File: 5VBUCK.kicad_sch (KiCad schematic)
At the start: 1 part, among them U1 LM76005RNPR

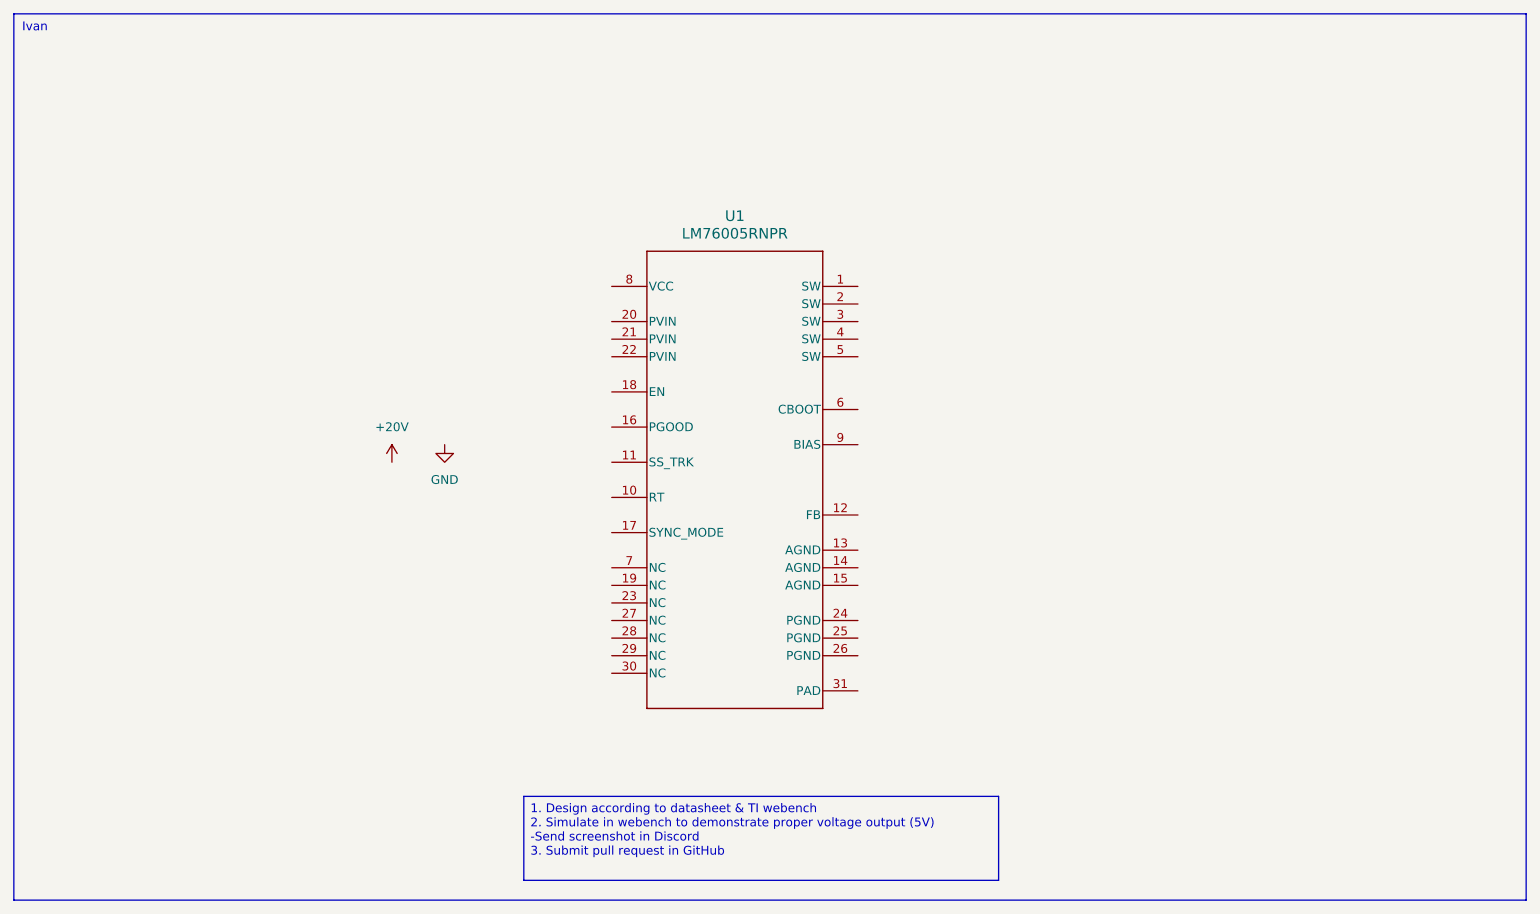
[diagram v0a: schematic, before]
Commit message: Complete 5V buck converter schematic
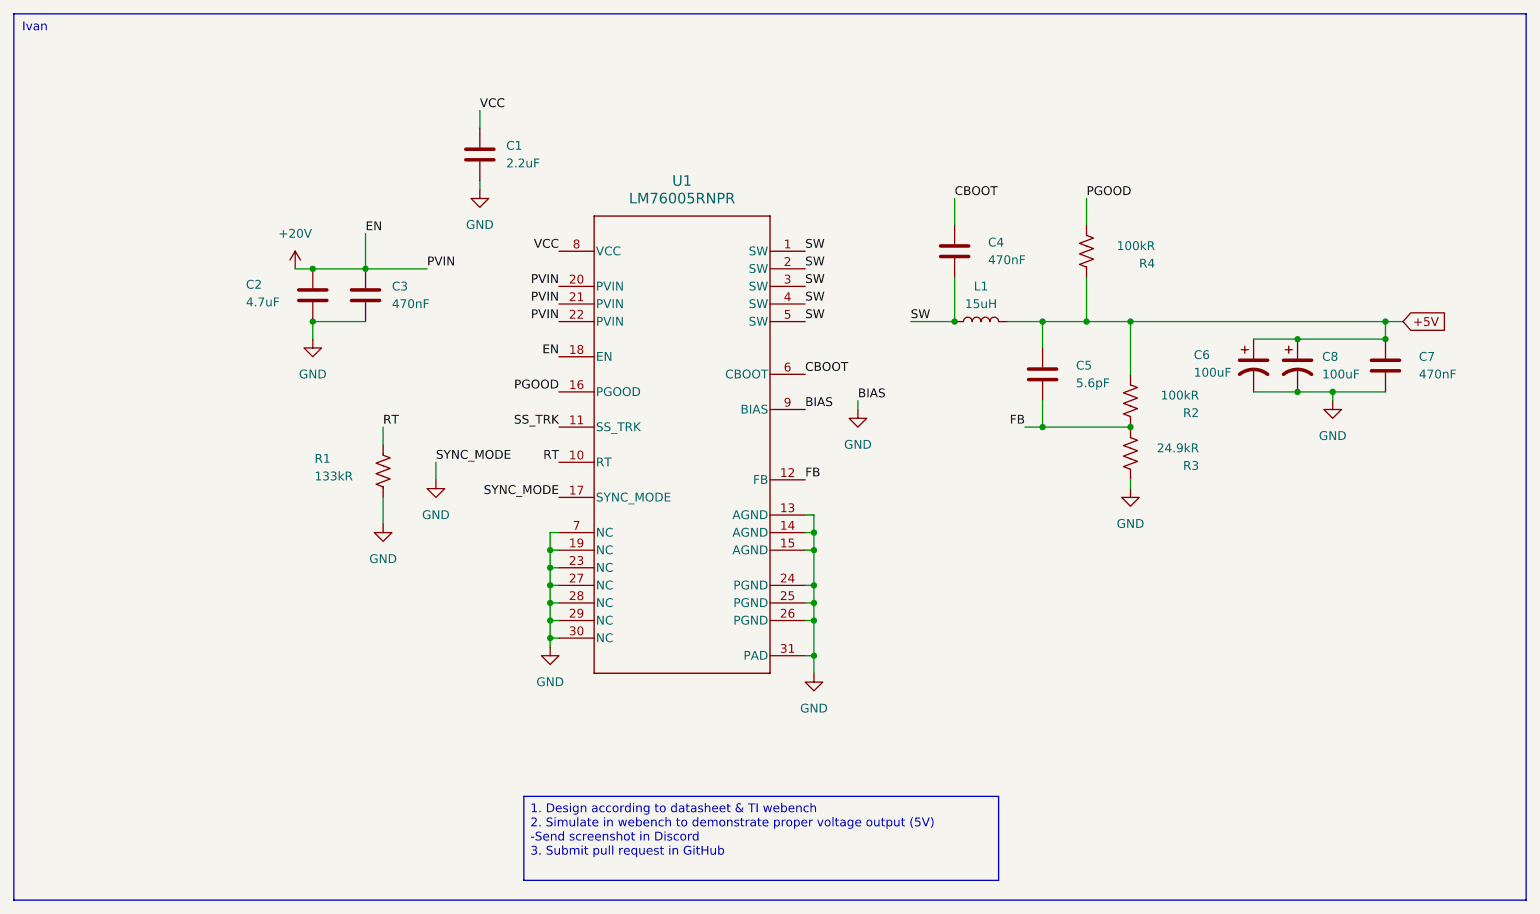
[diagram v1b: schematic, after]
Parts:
- added C1: 2.2uF, symbol Device:C
- added C2: 4.7uF, symbol Device:C
- added C3, C4, C7: 470nF, symbol Device:C
- added C5: 5.6pF, symbol Device:C
- added C6, C8: 100uF, symbol Device:C_Polarized_US
- added L1: 15uH, symbol Device:L
- added R1: 133kR, symbol Device:R_US
- added R2, R4: 100kR, symbol Device:R_US
- added R3: 24.9kR, symbol Device:R_US
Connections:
- net +20V: now also U1.18 (EN), U1.20 (PVIN), U1.21 (PVIN), U1.22 (PVIN), C2.1, C3.1
- net GND: now also U1.13 (AGND), U1.14 (AGND), U1.15 (AGND), U1.17 (SYNC_MODE), U1.19 (NC), U1.23 (NC), U1.24 (PGND), U1.25 (PGND), U1.26 (PGND), U1.27 (NC), U1.28 (NC), U1.29 (NC), U1.30 (NC), U1.31 (PAD), U1.7 (NC), U1.9 (BIAS), C1.2, C2.2, C3.2, C6.2, C7.2, C8.2, R1.2, R3.1
- net SW: now reaches U1.1 (SW)
- net SW: now also U1.2 (SW), U1.3 (SW), U1.4 (SW), U1.5 (SW), C4.2, L1.1
- net RT: now reaches U1.10 (RT)
- net RT: now also R1.1
- net SS_TRK: now reaches U1.11 (SS_TRK)
- net FB: now reaches U1.12 (FB)
- net FB: now also C5.2, R2.1, R3.2
- net PGOOD: now reaches U1.16 (PGOOD)
- net PGOOD: now also R4.2
- net CBOOT: now reaches U1.6 (CBOOT)
- net CBOOT: now also C4.1
- net VCC: now reaches U1.8 (VCC)
- net VCC: now also C1.1
- new net +5V: C5.1, C6.1, C7.1, C8.1, L1.2, R2.2, R4.1

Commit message: Updated the wires and lables of 5V
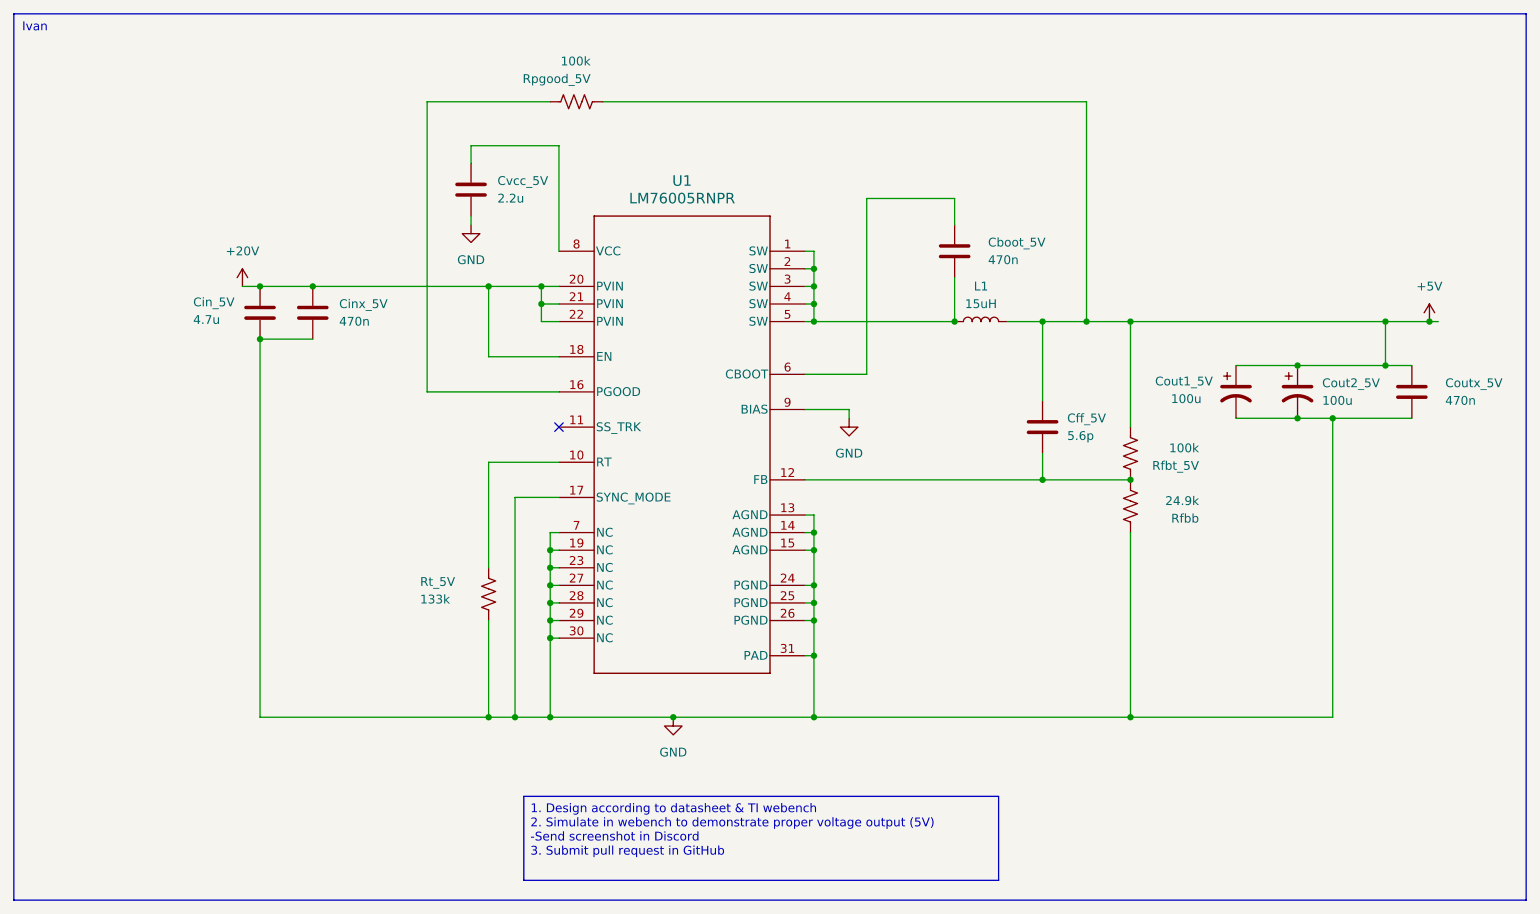
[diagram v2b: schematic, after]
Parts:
- Cboot_5V: renamed from C4; value 470nF -> 470n
- Cff_5V: renamed from C5; value 5.6pF -> 5.6p
- Cin_5V: renamed from C2; value 4.7uF -> 4.7u
- Cinx_5V: renamed from C3; value 470nF -> 470n
- Cout1_5V: renamed from C6; value 100uF -> 100u
- Cout2_5V: renamed from C8; value 100uF -> 100u
- Coutx_5V: renamed from C7; value 470nF -> 470n
- Cvcc_5V: renamed from C1; value 2.2uF -> 2.2u
- Rfbb: renamed from R3; value 24.9kR -> 24.9k
- Rfbt_5V: renamed from R2; value 100kR -> 100k
- Rpgood_5V: renamed from R4; value 100kR -> 100k
- Rt_5V: renamed from R1; value 133kR -> 133k
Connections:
- net +5V: now also Rpgood_5V.2; no longer Rpgood_5V.1
- net CBOOT: no longer names the net of Cboot_5V.1, U1.6 (CBOOT)
- net FB: no longer names the net of Cff_5V.2, Rfbb.2, Rfbt_5V.1, U1.12 (FB)
- net PGOOD: no longer names the net of U1.16 (PGOOD)
- net PGOOD: now also Rpgood_5V.1; no longer Rpgood_5V.2
- net RT: no longer names the net of Rt_5V.1, U1.10 (RT)
- net SS_TRK: no longer names the net of U1.11 (SS_TRK)
- net SW: no longer names the net of Cboot_5V.2, L1.1, U1.1 (SW), U1.2 (SW), U1.3 (SW), U1.4 (SW), U1.5 (SW)
- net VCC: no longer names the net of Cvcc_5V.1, U1.8 (VCC)
- no-connect marks 0 -> 1
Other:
- moved on the sheet: Cff_5V, Cin_5V, Cinx_5V, Cout1_5V, Cout2_5V, Coutx_5V, Cvcc_5V, Rfbb, Rfbt_5V, Rpgood_5V, Rt_5V

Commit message: Add complete layout-ready project files
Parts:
- removed Cout1_5V, Cout2_5V: 100u, symbol Device:C_Polarized_US
- removed L1: 15uH, symbol Device:L
- added Cout_5V_1, Cout_5V_2: 100u, BulkCapacitor_100u:CAP_EEFK_F_PAN, symbol BulkCap_100u:EEE-FP1V101AP
- added L1_5V1: 15u, Inductor_8.2u:IND_1217AS-H-150M=P3, symbol Inductor_8.2u:1217AS-H-150M=P3
- Cboot_5V1: renamed from Cboot_5V; footprint (none) -> Capacitor_SMD:C_0805_2012Metric
- Cff_5V1: renamed from Cff_5V; footprint (none) -> Capacitor_SMD:C_0603_1608Metric
- Cin_5V1: renamed from Cin_5V; footprint (none) -> Capacitor_SMD:C_0805_2012Metric
- Cinx_5V1: renamed from Cinx_5V; footprint (none) -> Capacitor_SMD:C_0805_2012Metric
- Coutx_5V1: renamed from Coutx_5V; footprint (none) -> Capacitor_SMD:C_0805_2012Metric
- Cvcc_5V1: renamed from Cvcc_5V; footprint (none) -> Capacitor_SMD:C_0603_1608Metric
- Rfbb1: renamed from Rfbb; footprint (none) -> Resistor_SMD:R_0603_1608Metric
- Rfbt_5V1: renamed from Rfbt_5V; footprint (none) -> Resistor_SMD:R_0603_1608Metric
- Rpgood_5V1: renamed from Rpgood_5V; footprint (none) -> Resistor_SMD:R_0603_1608Metric
- Rt_5V1: renamed from Rt_5V; footprint (none) -> Resistor_SMD:R_0603_1608Metric
- U3: renamed from U1; footprint RNP0030A -> Regulator:RNP0030A
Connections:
- net +5V: now also Cout_5V_1.1, Cout_5V_2.1, L1_5V1.2
- net GND: now also Cout_5V_1.2, Cout_5V_2.2
- net at Cboot_5V1.2, U3.1 (SW), U3.2 (SW)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: now also L1_5V1.1
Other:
- moved on the sheet: Cboot_5V1, Cff_5V1
